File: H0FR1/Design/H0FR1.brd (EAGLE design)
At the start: 34.6 x 30 mm, 25 parts, among them J1 CON-PHOENIX-350_1755749, K1 G5LE-14_DC3, P1 HEXABIT_17.32_NO_P6, Q1 MMBT3904LT1, U1 STM32G0B1CEU6N, X1 XTALL_CSTCE8M00G52

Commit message: Design modification
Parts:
- added C1, C10: 100nF, HEXABITZ_RCLS:C-0402
- added C11, C12: 330nF, HEXABITZ_RCLS:B32922Q_(18_X_8.5)
- added C9: 100nF, HEXABITZ_RCLS:C-0603
- added D4: MMSZ4705T1G, HEXABITZ_RCLS:SOD3716X135N
- added D5: BOURNS_CDSOD323-T03SCBOURNS_CDSOD323-T03SC_0_0, HEXABITZ_RCLS:BOURNS_CDSOD323-T03SC_0
- added R15: 10k, HEXABITZ_RCLS:R-0402
- added R7: 0.0R, HEXABITZ_RCLS:R-0603
- added R9: 150, HEXABITZ_RCLS:R-0402
- added TRIMBLE-LOGO1, TRIMBLE-LOGO2: HEXA-LOGO, HEXABITZ_USER_INTERFACE_PARTS:HEXA-LOGO
- added Z1, Z2: MMSZ5231BT3G, HEXABITZ_RCLS:SOD3716X135N@1
- C2, C4: device HEXABITZ_RCLS:C-0402 -> HEXABITZ_RCLS:C-0603-POL
- C5: device HEXABITZ_RCLS:C-0402 -> HEXABITZ_RCLS:C-0603
- C6: value 100nF -> 4.7uF; device HEXABITZ_RCLS:C-0402 -> HEXABITZ_RCLS:C-0603-POL
- C7: value 4.7uF -> 100nF
- FB1: value FB-TDK_MMZ1608Y300B -> (none); device HEXABITZ_RCLS:FB-TDK_MMZ1608Y300B -> HEXABITZ_RCLS:FB-0603
- Q1: value MMBT3904LT1 -> BSS123; device HEXABITZ_RCLS:MMBT3904LT1 -> HEXABITZ_RCLS:SOT23
- R2: value 180.0 Ω -> 180
- R3: value 10K -> 10k
- R4: value 1000 Ω -> 150
- R5: value 10.0 Ω -> 330; device HEXABITZ_RCLS:R-0402 -> HEXABITZ_RCLS:R2512
- R6: value 0.0R -> 330; device HEXABITZ_RCLS:R-0402 -> HEXABITZ_RCLS:R2512
- SWD: device pinhead:1X03 -> HEXABITZ_CONNECTION_PARTS:SWD
- moved R6 187.5 mm to (-17.0, -169.7), flipped to the top
- moved R5 158.3 mm to (-17.0, -138.0), flipped to the top
- moved C7 127.6 mm to (-19.4, -110.0), flipped to the top, turned to 0 degrees
- moved R4 124.8 mm to (-19.2, -105.9), flipped to the top
- moved Q1 98.1 mm to (-14.9, -78.7), flipped to the top
- moved FB1 61.8 mm to (-11.9, -43.0), flipped to the top, turned to 0 degrees
- moved C5 55.4 mm to (-15.9, -38.4), flipped to the top, turned to 0 degrees
- moved D2 51.6 mm to (0.00, -31.9), flipped to the top, turned to 180 degrees
- moved C6 47.6 mm to (-15.7, -29.2), flipped to the top, turned to 0 degrees
- moved C2 46.0 mm to (-9.53, -29.2), flipped to the top, turned to 0 degrees
- moved C3 45.1 mm to (-10.5, -33.8), flipped to the top, turned to 0 degrees
- moved R3 34.9 mm to (-15.7, -18.4), flipped to the top, turned to 0 degrees
- moved C4 34.3 mm to (-11.6, -22.9), flipped to the top, turned to 0 degrees
- moved SWD 30.6 mm to (-12.9, -15.2), turned to 0 degrees
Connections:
- net N$3 renamed LED_INDICATOR
- removed net N$10: J1.1, K1.4
- removed net N$117: U1.1
- removed net N$13: J1.3, K1.1
- removed net N$7: J1.2, K1.3
- new net COMMON: J1.3, K1.1, R5.1, R6.1
- new net N$12: C12.2, R6.2
- new net N$17: K1.5
- new net N$3: Q1.1, R15.1, R9.1, Z1.1
- new net N$9: C11.2, R5.2
- new net NORMALLY_CLOSED: C12.1, J1.1, K1.4
- new net NORMALLY_OPENED: C11.1, J1.2, K1.3
- new net RELAY_CONTROL: R9.2
- new net VREF: C1.1, C2.1
- net GND: now also D4.2, D5.2, R15.2, R7.1, Z2.1; no longer R6.1
- net N$1: now also Z1.2, Z2.2; no longer D3.+, K1.5, R5.2
- net N$11: now also C10.1, R4.1; no longer Q1.1, R4.2
- net N$15: now also C10.2, D3.+, D4.1; no longer R5.1
- net SSR: no longer R4.1
- net VDD: now also D5.1, FB1.1, R4.2; no longer FB1.2
- net VDDA: now also FB1.2; no longer C2.1, C7.1, FB1.1
- net VSSA: now also C1.2, R7.2; no longer C7.2, R6.2
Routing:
- net N$8: track 0.82 -> 50.8 mm
- net VDD: track 23.8 -> 1.14 mm, vias 3 -> 0
- net GND: track 58.1 -> 36.4 mm
- net CLK: track 12.1 -> 0.00 mm
- net DATA: track 10.1 -> 0.00 mm
- net N$1: track 4.26 -> 0.00 mm
- net N$15: track 2.11 -> 0.00 mm
- net LED_INDICATOR: track 7.52 -> 6.13 mm
- net VSSA: track 4.21 -> 3.27 mm
- net N$11: track 0.79 -> 0.00 mm

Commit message: Schematic modification
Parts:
- removed C11, C12: 330nF, HEXABITZ_RCLS:B32922Q_(18_X_8.5)
- removed R15: 10k, HEXABITZ_RCLS:R-0402
- removed Z1, Z2: MMSZ5231BT3G, HEXABITZ_RCLS:SOD3716X135N@1
- added D6, D7: MMSZ5231BT3G, HEXABITZ_RCLS:SOD3716X135N@1
- added R8: 10k, HEXABITZ_RCLS:R-0402
- C10: value 100nF -> 330nF; device HEXABITZ_RCLS:C-0402 -> HEXABITZ_RCLS:B32922Q_(18_X_8.5)
- C9: value 100nF -> 330nF; device HEXABITZ_RCLS:C-0603 -> HEXABITZ_RCLS:B32922Q_(18_X_8.5)
- moved R5 131.6 mm to (27.1, -14.0)
- moved R6 131.6 mm to (27.1, -45.7)
- moved D4 131.6 mm to (30.2, 0.64)
- moved R4 131.6 mm to (24.9, 18.1)
- moved C7 122.9 mm to (7.14, 10.0), flipped to the bottom, turned to 90 degrees
- moved C9 100.4 mm to (29.1, -26.7)
- moved C10 94.1 mm to (26.2, -36.8)
- moved R9 53.6 mm to (10.2, -10.0)
- moved Q1 53.6 mm to (11.0, -31.8)
- moved C8 18.4 mm to (24.8, 4.76), flipped to the top, turned to 0 degrees
- renumbered K1 to U2
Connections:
- removed net SSR: U1.45
- net GND: now also C7.2, D7.1, R8.2; no longer C8.2, R15.2, Z2.1
- net N$1: now also D6.2, D7.2; no longer Z1.2, Z2.2
- net N$11: now also C8.1; no longer C10.1
- net N$12: now also C10.2; no longer C12.2
- net N$15: now also C8.2; no longer C10.2
- net N$3: now also D6.1, R8.1; no longer R15.1, Z1.1
- net N$4: now also C7.1; no longer C8.1
- net N$9: now also C9.2; no longer C11.2
- net NORMALLY_CLOSED: now also C10.1; no longer C12.1
- net NORMALLY_OPENED: now also C9.1; no longer C11.1
- net RELAY_CONTROL: now also U1.45
- net VDD: no longer D2.A, D3.-, R4.2, U2.2
- net VDDA: now also D2.A, D3.-, R4.2, U2.2
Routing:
- net GND: track 36.4 -> 33.3 mm
- net SSR: track 2.85 -> 0.00 mm
- net RELAY_CONTROL: track 0.00 -> 2.85 mm

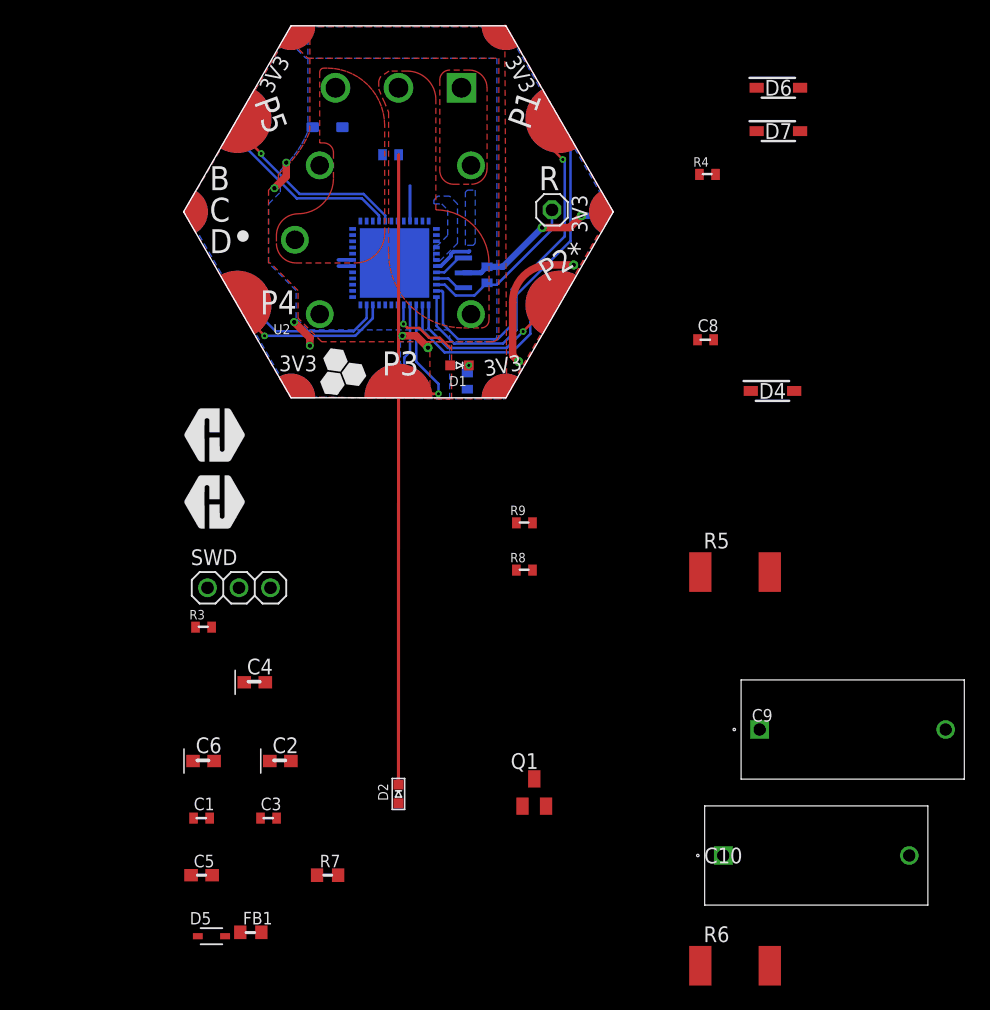
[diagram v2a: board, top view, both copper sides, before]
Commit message: Intial parts placing on the board
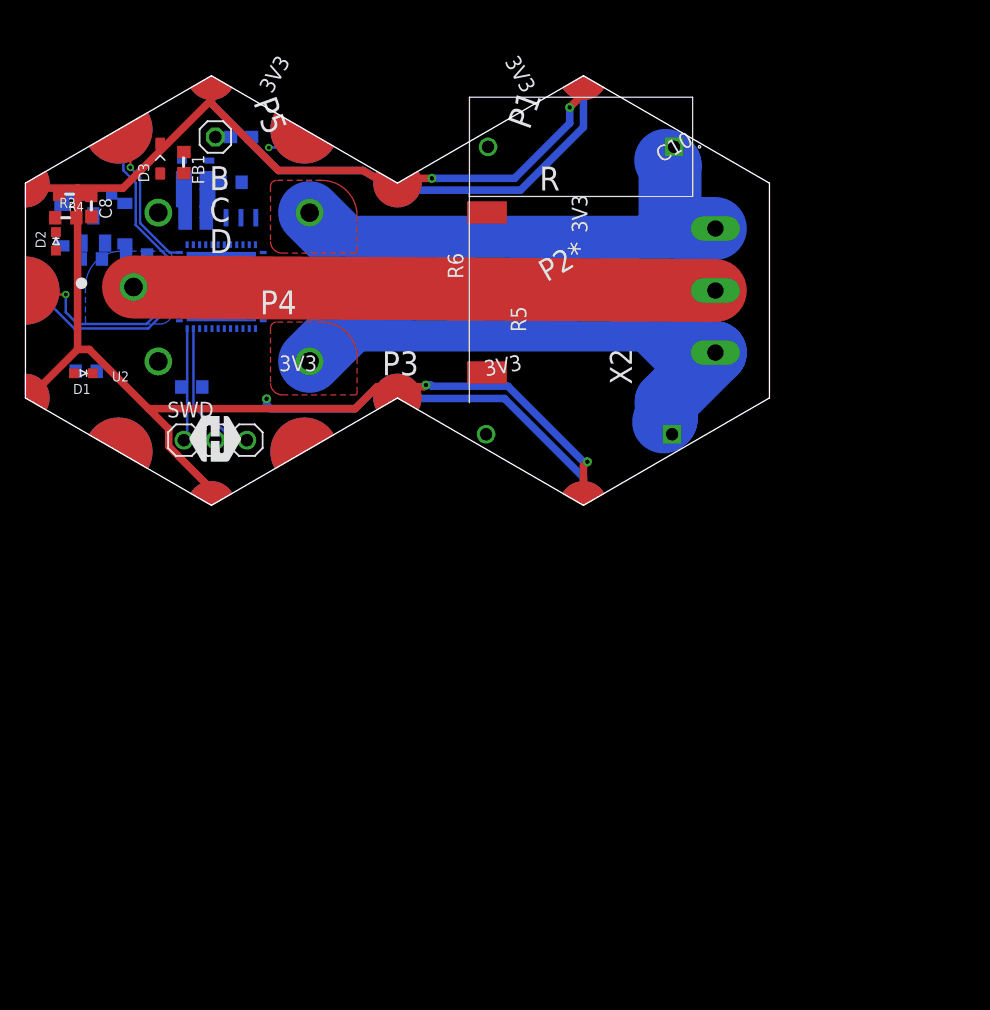
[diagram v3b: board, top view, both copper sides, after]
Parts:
- removed C3: 100nF, HEXABITZ_RCLS:C-0402
- removed C4: 4.7uF, HEXABITZ_RCLS:C-0603-POL
- removed J1: CON-PHOENIX-350_1755749, Hexabitz:SHDR3W100P0X508_1X3_1724X860X1
- removed TRIMBLE-LOGO1: HEXA-LOGO, HEXABITZ_USER_INTERFACE_PARTS:HEXA-LOGO
- added X2: (no value), HEXABITZ_CONNECTION_PARTS:AK300/3
- C1, C7, C8: device HEXABITZ_RCLS:C-0402 -> HEXABITZ_RCLS:C-0603
- C2, C6: device HEXABITZ_RCLS:C-0603-POL -> HEXABITZ_RCLS:C-0805
- D3: value SMD-DIODE-SCHOTTKY-40V-300MA(SOD-323) -> 40V 300MA; device Hexabitz:SOD-323 -> HEXABITZ_RCLS:SOD-323
- D4: value MMSZ4705T1G -> MMSZ4705T1GMMSZ4705T1G; device HEXABITZ_RCLS:SOD3716X135N -> HEXABITZ_RCLS:DIO_MMSZ4700T1G
- D6, D7: value MMSZ5231BT3G -> MMSZ4705T1GMMSZ4705T1G; device HEXABITZ_RCLS:SOD3716X135N@1 -> HEXABITZ_RCLS:DIO_MMSZ4700T1G
- P1: value HEXABIT_17.32_NO_P6 -> HEXABIT_X2_P1_P5_EDIT_POWER_PADS; device hexabitz_connectors:HEXABIT_17.32_NO_P6 -> hexabitz_connectors:HEXABIT_X2_P1_P5_EDIT_POWER_PADS
- R1, R2, R3, R4, R8, R9: device HEXABITZ_RCLS:R-0402 -> HEXABITZ_RCLS:R-0603
- U1: value STM32G0B1CEU6N -> STM32G0B1CEU6QFN_B1CEU6_STM-L; device HEXABITZ_ICs:HEXABITZ_ICS_QFN_B1CEU6_STM-L -> HEXABITZ_ICs:QFN_B1CEU6_STM-L
- moved D5 62.6 mm to (-16.4, 19.2), flipped to the bottom, turned to 180 degrees
- moved FB1 62.3 mm to (-17.3, 19.1), turned to 270 degrees
- moved R6 61.3 mm to (7.14, 12.2), turned to 90 degrees
- moved D4 58.8 mm to (-27.1, 14.0), flipped to the bottom, turned to 90 degrees
- moved Q1 57.7 mm to (-24.6, 13.7), flipped to the bottom
- moved C10 57.3 mm to (22.2, 20.3), turned to 180 degrees
- moved R7 56.4 mm to (-13.5, 17.5), flipped to the bottom
- moved D7 55.6 mm to (-24.8, 16.7), flipped to the bottom, turned to 180 degrees
- moved D6 53.8 mm to (-22.1, 14.1), flipped to the bottom, turned to 90 degrees
- moved C5 52.5 mm to (-16.4, 14.1), flipped to the bottom, turned to 180 degrees
- moved D2 52.4 mm to (-27.6, 12.7)
- moved R4 51.5 mm to (-26.5, 16.5), turned to 180 degrees
- moved C8 50.7 mm to (-24.8, 15.6), turned to 270 degrees
- moved C1 48.9 mm to (-16.4, 15.1), flipped to the bottom, turned to 180 degrees
- moved C2 47.3 mm to (-16.3, 17.6), flipped to the bottom, turned to 180 degrees
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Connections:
- removed net N$17: U2.5
- removed net VREF: C1.1, C2.1
- net COMMON: now also X2.2; no longer J1.3
- net GND: now also D4.A, D7.K, P1.PAD_PD13, P1.PAD_PD14, P1.PAD_PD17, P1.PAD_PD18, P1.PAD_PD19, P1.PAD_PD20; no longer C3.2, C4.2, D4.2, D7.1, P1.PAD_PD10, P1.PAD_PD7, P1.PAD_PD8, P1.PAD_PD9, U1.30
- net N$1: now also D6.A, D7.A; no longer D6.2, D7.2
- net N$15: now also D4.K, U2.5; no longer D4.1
- net N$3: now also D6.K; no longer D6.1
- net NORMALLY_CLOSED: now also X2.3; no longer J1.1
- net NORMALLY_OPENED: now also X2.1; no longer J1.2
- net USART4_RX: no longer P1.PAD_PD1
- net USART4_TX: no longer P1.PAD_PU1
- net USART6_RX: now also P1.PAD_PD1, U1.47; no longer U1.16
- net USART6_TX: now also P1.PAD_PU1, U1.48; no longer U1.15
- net VDD: now also D2.A, D3.-, P1.PAD_PU13, P1.PAD_PU14, P1.PAD_PU17, P1.PAD_PU18, P1.PAD_PU19, P1.PAD_PU20, R4.2, U2.2; no longer C3.1, C4.1, P1.PAD_PU10, P1.PAD_PU7, P1.PAD_PU8, P1.PAD_PU9, U1.31
- net VDDA: now also C1.1, C2.1; no longer D2.A, D3.-, R4.2, U2.2
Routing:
- net VDD: track 1.14 -> 132.6 mm, vias 0 -> 4
- net N$8: track 50.8 -> 0.00 mm
- net COMMON: track 0.00 -> 46.9 mm
- net NORMALLY_OPENED: track 0.00 -> 42.5 mm
- net NORMALLY_CLOSED: track 0.00 -> 40.2 mm
- net GND: track 33.3 -> 71.4 mm, vias 10 -> 1
- net USART4_RX: track 28.9 -> 0.00 mm
- net USART4_TX: track 28.2 -> 0.00 mm, vias 1 -> 0
- net USART2_TX: track 14.2 -> 0.00 mm, vias 1 -> 0
- net USART3_TX: track 13.9 -> 0.00 mm, vias 1 -> 0
- net N$4: track 13.7 -> 0.00 mm
- net USART2_RX: track 15.5 -> 2.88 mm, vias 0 -> 1
- net USART3_RX: track 12.4 -> 0.00 mm
- net DATA: track 0.00 -> 11.7 mm
- net CLK: track 0.00 -> 11.6 mm
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- added copper zone on layer 16, net VDD
- removed copper zone on layer 16, net GND
- removed copper zone on layer 1, net N$10
- removed copper zone on layer 1, net N$13
- removed copper zone on layer 1, net N$7
- removed copper zone on layer 16, net VDDA
- removed copper zone on layer 16, net VSSA
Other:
- board size 34.6 x 30 mm -> 60 x 34.6 mm
